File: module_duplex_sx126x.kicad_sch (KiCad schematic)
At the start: 38 parts, among them J1 USB_B_Mini, J2 Conn_01x06_Pin, J3 Conn_01x05, J4 Conn_01x04, J5 Conn_01x02_Pin, J6 Conn_01x02, SW1 SW_Push, U1 STM32F103C8Tx, U2 AMS1117-3.3, U3 SN65HVD230, U4 Ai-Thinker-Ra-02, U5 Ai-Thinker-Ra-02, Y1 16M, Y2 32.768k

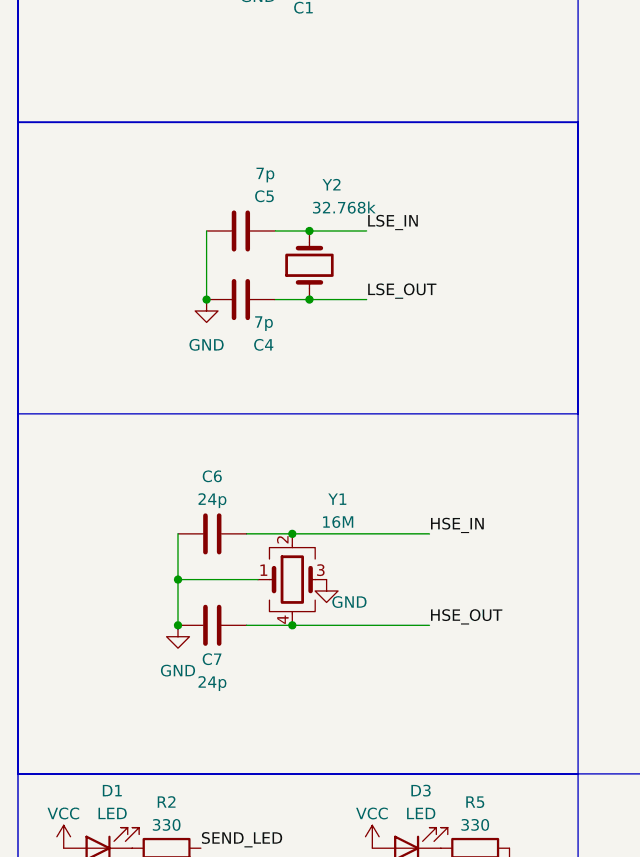
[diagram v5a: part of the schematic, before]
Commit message: Added LCSC part numbers for production
Signed-off-by: Leonardo Celente <leocelente@gmail.com>
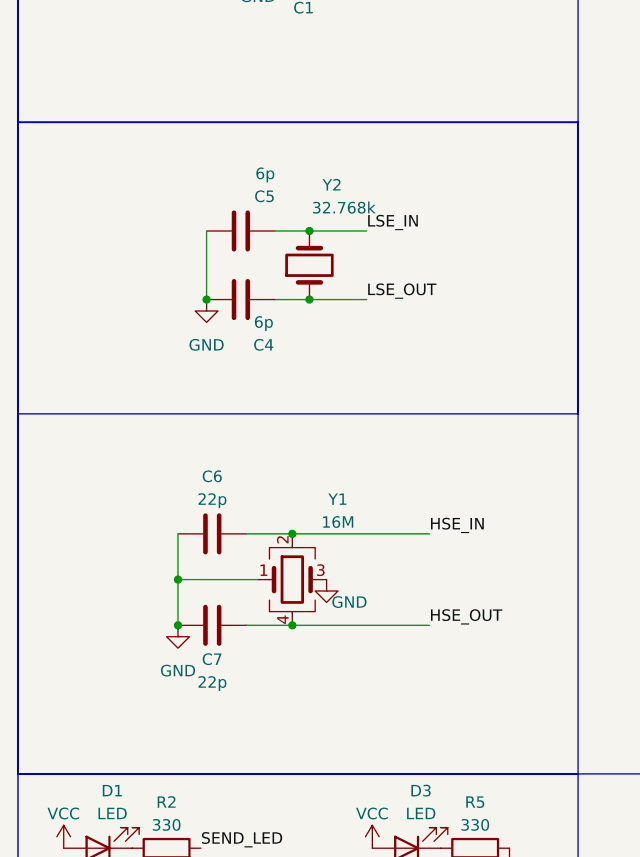
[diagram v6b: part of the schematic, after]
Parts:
- C1, C10, C11, C12, C2: LCSC (none) -> C14663
- C13, C14, C8, C9: LCSC (none) -> C19666
- C3: LCSC (none) -> C57112
- C4, C5: value 7p -> 6p; LCSC (none) -> C37474
- C6, C7: value 24p -> 22p; LCSC (none) -> C1653
- D1: LCSC (none) -> C72043
- D2: LCSC (none) -> C72041
- D3: LCSC (none) -> C2286
- H1, H2, J1, J2, J3, J4, J5, J6, U4, U5: now left out of the parts list
- R1, R4: LCSC (none) -> C23345
- R2, R3, R5: LCSC (none) -> C23138
- SW1: LCSC (none) -> C318884
- U1: LCSC (none) -> C8734
- U2: LCSC (none) -> C6186
- U3: LCSC (none) -> C12084
- Y1: LCSC (none) -> C13738
- Y2: LCSC (none) -> C32346
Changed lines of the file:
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@@
+      (effects (font (size 1.27 1.27)) hide)
+    )
+    (property "LCSC" "C72043" (at 20.32 174.625 0)
       (effects (font (size 1.27 1.27)) hide)
     )
@@
   )
   (symbol (lib_id "RF_Module:Ai-Thinker-Ra-02") (at 229.87 81.28 0) (unit 1)
-    (in_bom yes) (on_board yes) (dnp no) (fields_autoplaced)
+    (in_bom no) (on_board yes) (dnp no) (fields_autoplaced)
     (property "Reference" "U4" (at 231.8259 64.77 0)
       (effects (font (size 1.27 1.27)) (justify left))
@@
       (effects (font (size 1.27 1.27)) hide)
     )
+    (property "LCSC" "C14663" (at 53.34 41.91 0)
+      (effects (font (size 1.27 1.27)) hide)
+    )
     (pin "1")
     (pin "2")
@@
       (effects (font (size 1.27 1.27)) hide)
     )
+    (property "LCSC" "C57112" (at 31.75 41.91 0)
+      (effects (font (size 1.27 1.27)) hide)
+    )
     (pin "1")
     (pin "2")
@@
       (effects (font (size 1.27 1.27)) hide)
     )
+    (property "LCSC" "C23138" (at 62.23 174.625 90)
+      (effects (font (size 1.27 1.27)) hide)
+    )
     (pin "1")
     (pin "2")
@@
       (effects (font (size 1.27 1.27)) hide)
     )
+    (property "LCSC" "C19666" (at 73.66 41.91 0)
+      (effects (font (size 1.27 1.27)) hide)
+    )
     (pin "1")
     (pin "2")
@@
       (effects (font (size 1.27 1.27)) hide)
     )
+    (property "LCSC" "C14663" (at 63.5 41.91 0)
+      (effects (font (size 1.27 1.27)) hide)
+    )
     (pin "1")
     (pin "2")
@@
   )
   (symbol (lib_id "Connector_Generic:Conn_01x04") (at 240.03 27.94 0) (unit 1)
-    (in_bom yes) (on_board yes) (dnp no)
+    (in_bom no) (on_board yes) (dnp no)
     (property "Reference" "J4" (at 241.935 34.925 0)
       (effects (font (size 1.27 1.27)) (justify left))
@@
       (effects (font (size 1.27 1.27)) hide)
     )
+    (property "LCSC" "C72041" (at 20.955 189.23 0)
+      (effects (font (size 1.27 1.27)) hide)
+    )
     (pin "1")
     (pin "2")
@@
     )
     (property "Datasheet" "http://www.ti.com/lit/ds/symlink/sn65hvd230.pdf" (at 162.56 16.51 0)
+      (effects (font (size 1.27 1.27)) hide)
+    )
+    (property "LCSC" "C12084" (at 165.1 26.67 0)
       (effects (font (size 1.27 1.27)) hide)
     )
@@
       (effects (font (size 1.27 1.27)) (justify left))
     )
-    (property "Value" "7p" (at 40.005 99.695 90)
+    (property "Value" "6p" (at 40.005 99.695 90)
       (effects (font (size 1.27 1.27)) (justify left))
     )
@@
       (effects (font (size 1.27 1.27)) hide)
     )
+    (property "LCSC" "C37474" (at 36.195 106.045 90)
+      (effects (font (size 1.27 1.27)) hide)
+    )
     (pin "1")
     (pin "2")
@@
       (effects (font (size 1.27 1.27)) hide)
     )
+    (property "LCSC" "C23345" (at 127.635 33.02 90)
+      (effects (font (size 1.27 1.27)) hide)
+    )
     (pin "1")
     (pin "2")
@@
   )
   (symbol (lib_id "Connector:USB_B_Mini") (at 113.665 33.02 0) (unit 1)
-    (in_bom yes) (on_board yes) (dnp no) (fields_autoplaced)
+    (in_bom no) (on_board yes) (dnp no) (fields_autoplaced)
     (property "Reference" "J1" (at 113.665 21.59 0)
       (effects (font (size 1.27 1.27)))
@@
       (effects (font (size 1.27 1.27)) hide)
     )
+    (property "LCSC" "C2286" (at 54.61 174.625 0)
+      (effects (font (size 1.27 1.27)) hide)
+    )
     (pin "1")
     (pin "2")
@@
       (effects (font (size 1.27 1.27)) hide)
     )
+    (property "LCSC" "C318884" (at 43.18 72.39 0)
+      (effects (font (size 1.27 1.27)) hide)
+    )
     (pin "1")
     (pin "2")
@@
   )
   (symbol (lib_id "Mechanical:MountingHole") (at 219.71 173.99 0) (unit 1)
-    (in_bom yes) (on_board yes) (dnp no) (fields_autoplaced)
+    (in_bom no) (on_board yes) (dnp no) (fields_autoplaced)
     (property "Reference" "H2" (at 222.25 173.355 0)
       (effects (font (size 1.27 1.27)) (justify left))
@@
       (effects (font (size 1.27 1.27)) hide)
     )
+    (property "LCSC" "C19666" (at 83.82 41.91 0)
+      (effects (font (size 1.27 1.27)) hide)
+    )
     (pin "1")
     (pin "2")
@@
   )
   (symbol (lib_id "Connector_Generic:Conn_01x02") (at 180.34 45.72 0) (unit 1)
-    (in_bom yes) (on_board yes) (dnp no) (fields_autoplaced)
+    (in_bom no) (on_board yes) (dnp no) (fields_autoplaced)
     (property "Reference" "J6" (at 182.88 46.355 0)
       (effects (font (size 1.27 1.27)) (justify left))
@@
     )
     (property "Datasheet" "~" (at 41.91 144.78 0)
+      (effects (font (size 1.27 1.27)) hide)
+    )
+    (property "LCSC" "C13738" (at 41.91 144.78 0)
       (effects (font (size 1.27 1.27)) hide)
     )
@@
       (effects (font (size 1.27 1.27)) hide)
     )
+    (property "LCSC" "C23345" (at 127.635 35.56 90)
+      (effects (font (size 1.27 1.27)) hide)
+    )
     (pin "1")
     (pin "2")
@@
       (effects (font (size 1.27 1.27)))
     )
-    (property "Value" "24p" (at 33.02 156.21 90)
+    (property "Value" "22p" (at 33.02 156.21 90)
       (effects (font (size 1.27 1.27)))
     )
@@
       (effects (font (size 1.27 1.27)) hide)
     )
+    (property "LCSC" "C1653" (at 33.02 149.86 90)
+      (effects (font (size 1.27 1.27)) hide)
+    )
     (pin "1")
     (pin "2")
@@
       (effects (font (size 1.27 1.27)) hide)
     )
+    (property "LCSC" "C23138" (at 28.575 189.23 90)
+      (effects (font (size 1.27 1.27)) hide)
+    )
     (pin "1")
     (pin "2")
@@
       (effects (font (size 1.27 1.27)))
     )
-    (property "Value" "24p" (at 33.02 135.89 90)
+    (property "Value" "22p" (at 33.02 135.89 90)
       (effects (font (size 1.27 1.27)))
     )
@@
       (effects (font (size 1.27 1.27)) hide)
     )
+    (property "LCSC" "C1653" (at 33.02 139.7 90)
+      (effects (font (size 1.27 1.27)) hide)
+    )
     (pin "1")
     (pin "2")
@@
   )
   (symbol (lib_id "Connector_Generic:Conn_01x05") (at 218.44 29.21 0) (unit 1)
-    (in_bom yes) (on_board yes) (dnp no)
+    (in_bom no) (on_board yes) (dnp no)
     (property "Reference" "J3" (at 221.615 34.925 0)
       (effects (font (size 1.27 1.27)) (justify left))
@@
       (effects (font (size 1.27 1.27)) hide)
     )
+    (property "LCSC" "C14663" (at 43.18 74.93 90)
+      (effects (font (size 1.27 1.27)) hide)
+    )
     (pin "1")
     (pin "2")
@@
   )
   (symbol (lib_id "Connector:Conn_01x02_Pin") (at 257.175 31.75 180) (unit 1)
-    (in_bom yes) (on_board yes) (dnp no)
+    (in_bom no) (on_board yes) (dnp no)
     (property "Reference" "J5" (at 258.445 34.925 0)
       (effects (font (size 1.27 1.27)) (justify right))
@@
       (effects (font (size 1.27 1.27)) hide)
     )
+    (property "LCSC" "C14663" (at 21.59 41.91 0)
+      (effects (font (size 1.27 1.27)) hide)
+    )
     (pin "1")
     (pin "2")
@@
     )
     (property "Datasheet" "https://www.st.com/resource/en/datasheet/stm32f103c8.pdf" (at 121.92 107.95 0)
+      (effects (font (size 1.27 1.27)) hide)
+    )
+    (property "LCSC" "C8734" (at 121.92 107.95 0)
       (effects (font (size 1.27 1.27)) hide)
     )
@@
   )
   (symbol (lib_id "Connector:Conn_01x06_Pin") (at 280.035 31.115 180) (unit 1)
-    (in_bom yes) (on_board yes) (dnp no)
+    (in_bom no) (on_board yes) (dnp no)
     (property "Reference" "J2" (at 281.305 34.925 0)
       (effects (font (size 1.27 1.27)) (justify right))
@@
       (effects (font (size 1.27 1.27)) hide)
     )
+    (property "LCSC" "C23138" (at 27.94 174.625 90)
+      (effects (font (size 1.27 1.27)) hide)
+    )
     (pin "1")
     (pin "2")
@@
       (effects (font (size 1.27 1.27)) hide)
     )
+    (property "LCSC" "C19666" (at 66.04 25.4 0)
+      (effects (font (size 1.27 1.27)) hide)
+    )
     (pin "1")
     (pin "2")
@@
       (effects (font (size 1.27 1.27)) hide)
     )
+    (property "LCSC" "C32346" (at 43.815 109.855 90)
+      (effects (font (size 1.27 1.27)) hide)
+    )
     (pin "1")
     (pin "2")
@@
       (effects (font (size 1.27 1.27)) hide)
     )
+    (property "LCSC" "C6186" (at 58.42 21.59 0)
+      (effects (font (size 1.27 1.27)) hide)
+    )
     (pin "1")
     (pin "2")
@@
       (effects (font (size 1.27 1.27)) hide)
     )
+    (property "LCSC" "C14663" (at 41.91 41.91 0)
+      (effects (font (size 1.27 1.27)) hide)
+    )
     (pin "1")
     (pin "2")
@@
       (effects (font (size 1.27 1.27)) hide)
     )
+    (property "LCSC" "C19666" (at 50.8 25.4 0)
+      (effects (font (size 1.27 1.27)) hide)
+    )
     (pin "1")
     (pin "2")
@@
   )
   (symbol (lib_id "RF_Module:Ai-Thinker-Ra-02") (at 229.87 138.43 0) (unit 1)
-    (in_bom yes) (on_board yes) (dnp no) (fields_autoplaced)
+    (in_bom no) (on_board yes) (dnp no) (fields_autoplaced)
     (property "Reference" "U5" (at 231.8259 121.92 0)
       (effects (font (size 1.27 1.27)) (justify left))
@@
   )
   (symbol (lib_id "Mechanical:MountingHole") (at 201.295 173.99 0) (unit 1)
-    (in_bom yes) (on_board yes) (dnp no) (fields_autoplaced)
+    (in_bom no) (on_board yes) (dnp no) (fields_autoplaced)
     (property "Reference" "H1" (at 203.835 173.355 0)
       (effects (font (size 1.27 1.27)) (justify left))
@@
       (effects (font (size 1.27 1.27)))
     )
-    (property "Value" "7p" (at 38.735 116.205 90)
+    (property "Value" "6p" (at 38.735 116.205 90)
       (effects (font (size 1.27 1.27)))
     )
@@
       (effects (font (size 1.27 1.27)) hide)
     )
+    (property "LCSC" "C37474" (at 36.195 113.665 90)
+      (effects (font (size 1.27 1.27)) hide)
+    )
